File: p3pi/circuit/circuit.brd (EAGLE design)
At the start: 94 x 50.8 mm, 22 parts, among them IC1 TS 5205 CX533, Q1 BSS123, X1 STECKER_MICROMATCH_4SMD, X2 STECKER_MICROMATCH_4SMD

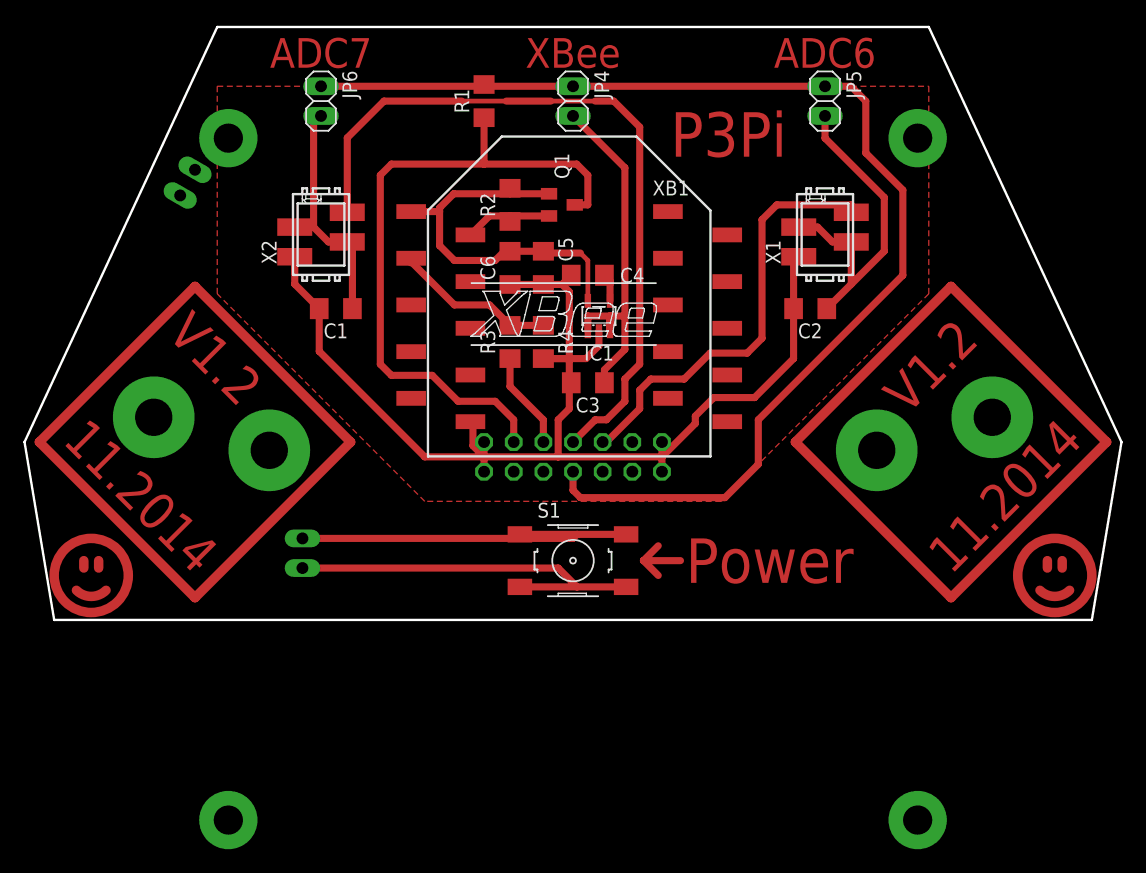
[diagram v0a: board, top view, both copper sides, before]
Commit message: update P3Pi to Version 1.3
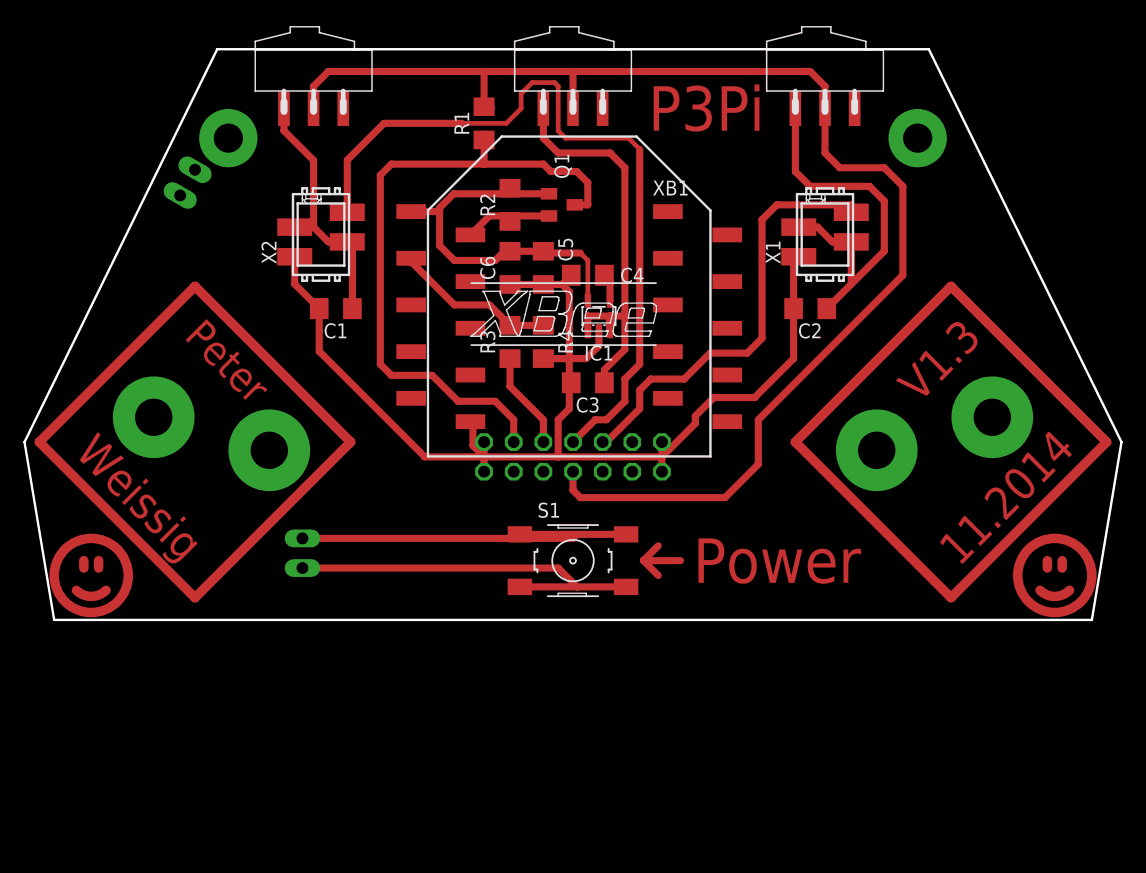
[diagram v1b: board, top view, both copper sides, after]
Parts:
- removed JP4, JP5, JP6: (no value), pinhead:1X02
- added S2, S3, S4: (no value), robo_ag:SCHALTER_SMD
- R3: value 10K -> 5K
- moved R1 1.91 mm to (43.2, 52.7)
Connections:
- net VCC: now also S2.C, S3.C, S4.C; no longer JP4.1, JP5.1, JP6.1
- net VCC_ADC6: now also S2.1; no longer JP6.2
- net VCC_ADC7: now also S3.1; no longer JP5.2
- net VCC_XBEE: now also S4.1; no longer JP4.2
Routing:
- net VCC: track 104.4 -> 115.3 mm
- net VCC_ADC7: track 29.3 -> 34.0 mm
- net VCC_XBEE: track 32.5 -> 36.8 mm
- net PD0_3PIRX: track 57.7 -> 55.4 mm
- net ADC6: track 63.6 -> 65.6 mm
- net VCC_ADC6: track 20.7 -> 22.1 mm
- removed copper zone on layer 1, net GND
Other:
- board size 94 x 50.8 mm -> 94 x 48.9 mm
- board text added: "Peter"
- board text added: "V1.3"
- board text added: "Weissig"
- board text removed: "ADC6"
- board text removed: "ADC7"
- board text removed: "V1.2"
- board text removed: "XBee"
